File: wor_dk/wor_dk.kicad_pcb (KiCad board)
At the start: 4 copper layers, 108.7 x 57.5 mm, 140 parts, among them J101 Conn_01x02, J102 Conn_02x03_Odd_Even, J103 Conn_02x03_Odd_Even, J104 Conn_01x02, J201 SWD, J301 SMA, J302 Conn_02x04_Odd_Even, J303 Conn_02x06_Odd_Even, J401 USB_C_Receptacle_USB2.0_16P, J501 SWD, J502 USB_C_Receptacle_USB2.0_16P, J503 SWD, Q501 BSS84, SW201 SW_Push, SW501 SW_Push, U201 nRF52840, U202 TMUX1112PWR, U203 TMUX1112PWR, U301 Si4467, U401 FT232RL, U501 TLV1117-33, U502 LPC11U35FHI33_501, Y201 32.768kHz, Y202 32MHz, Y301 26MHz, Y501 12MHz

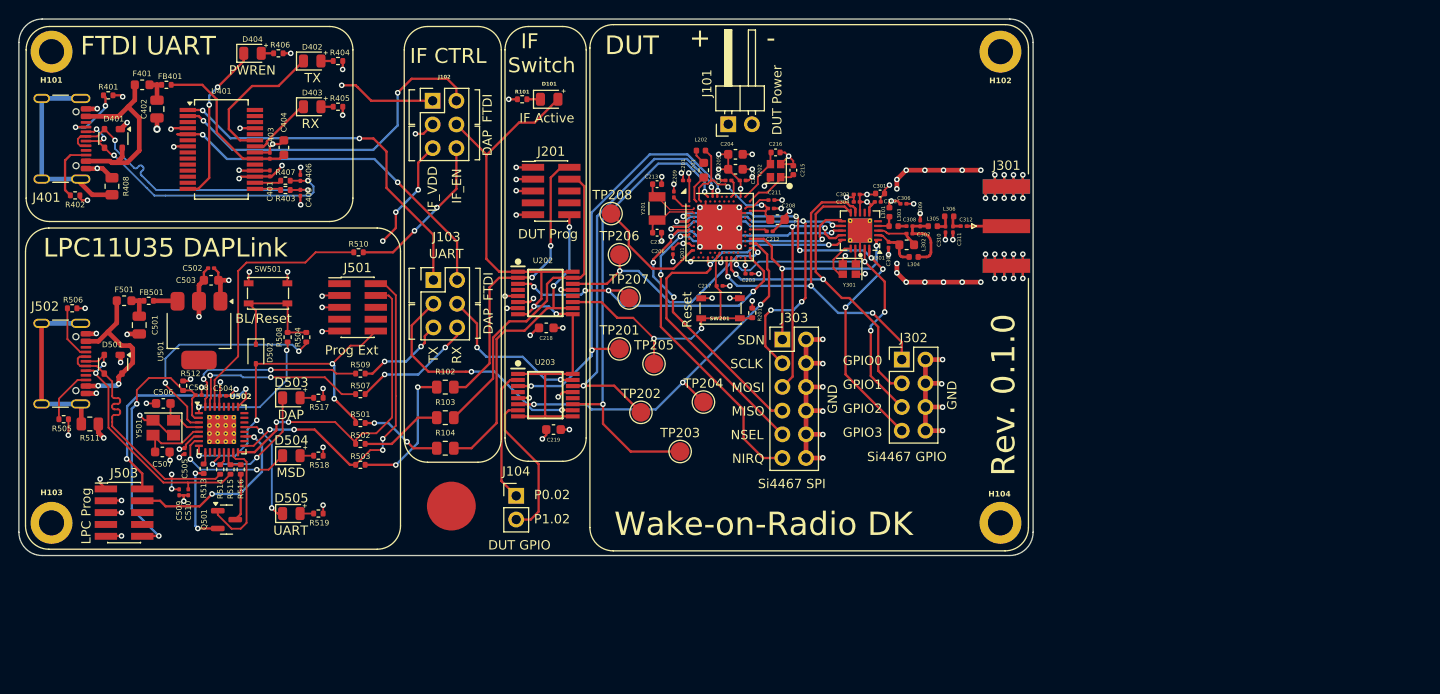
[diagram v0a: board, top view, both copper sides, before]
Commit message: wor_dk: PCB: adjust zone fills
- GND zone fill reduced to size of PCB
- VDD zone fills: chamfer corners
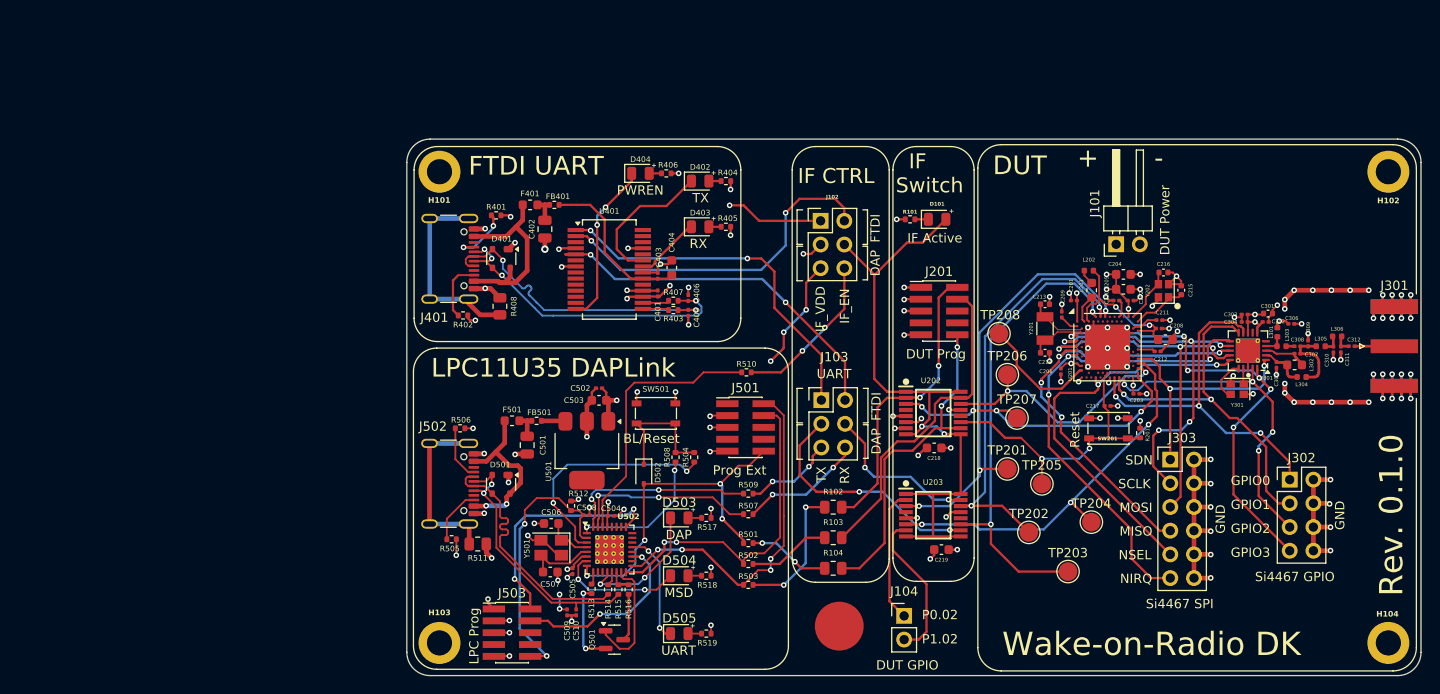
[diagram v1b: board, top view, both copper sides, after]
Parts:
- moved C213 43.5 mm to (165.4, 84.9)
- moved D504 43.5 mm to (126.2, 114.0)
- moved D505 43.5 mm to (126.2, 120.2)
- moved R510 43.5 mm to (133.4, 92.2)
- moved Y201 43.5 mm to (165.4, 87.5)
- moved H101 43.5 mm to (100.5, 70.7)
- moved H103 43.5 mm to (100.5, 121.2)
- moved C214 43.5 mm to (165.4, 90.1)
- moved C218 43.5 mm to (153.5, 100.3)
- moved D101 43.5 mm to (153.8, 75.8)
- moved D503 43.5 mm to (126.2, 107.8)
- moved FB401 43.5 mm to (112.8, 74.2)
- moved R401 43.5 mm to (106.6, 75.3)
- moved R406 43.5 mm to (124.8, 70.8)
- moved R514 43.5 mm to (118.6, 115.4)
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
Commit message: wor_dk: PCB: cleanup
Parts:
- moved TP203 5.01 mm to (163.1, 111.9)
- moved TP202 3.02 mm to (161.5, 107.2)
- moved R401 2.57 mm to (104.3, 74.1)
- moved TP205 1.00 mm to (166.0, 104.4)
- moved C404 0.84 mm to (125.3, 81.8)
- moved TP204 0.69 mm to (169.8, 107.8)
- moved L202 0.62 mm to (170.7, 81.3)
- moved J201 0.53 mm to (153.5, 85.6)
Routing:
- net /Main MCU/P0.31_: track 50.6 -> 43.6 mm
- net Net-(D402-K): track 15.6 -> 11.3 mm
- net /Main MCU/P0.29_: track 44.6 -> 40.6 mm
- net /LPC11U35 DAPLink Programmer/USB-SCON: track 13.1 -> 9.87 mm, vias 0 -> 2
- net /3V3_FTDI: track 20.1 -> 17.7 mm, vias 7 -> 6
- net /RXD_FTDI: track 39.9 -> 37.7 mm
- net /LPC11U35 DAPLink Programmer/IF_SWDIO: track 25.4 -> 23.7 mm
- net /Main MCU/SWCLK_: track 26.8 -> 25.6 mm
- net /Main MCU/SWDIO_: track 35.0 -> 33.8 mm
- net Net-(D404-K): track 17.7 -> 18.7 mm
- net Net-(J401-CC1): track 6.62 -> 7.64 mm, vias 2 -> 0
- net /Transceiver/MISO: track 47.2 -> 48.0 mm
- net /DTR_FTDI: track 37.3 -> 36.5 mm
- net /Main MCU/NRESET_: track 32.6 -> 33.3 mm
- net Net-(U401-VCC): track 17.6 -> 18.3 mm
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
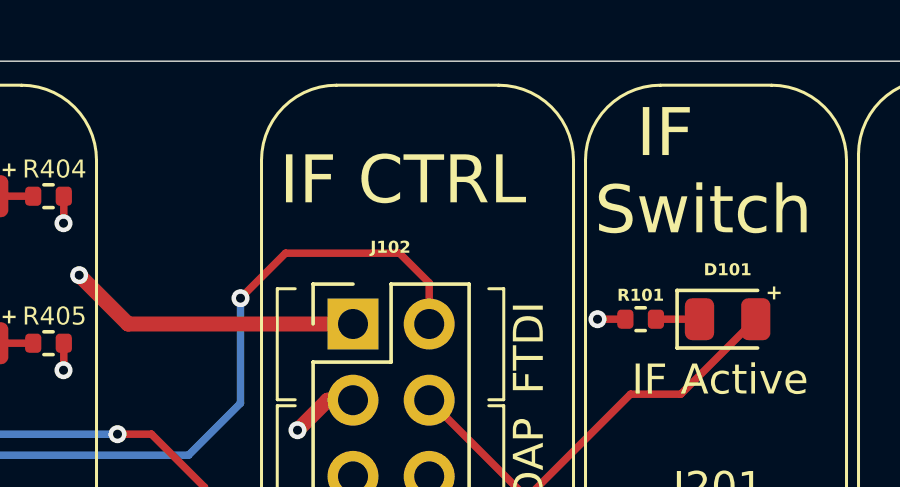
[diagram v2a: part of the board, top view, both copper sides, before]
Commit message: wor_dk: PCB: IF CTRL -> IF Control
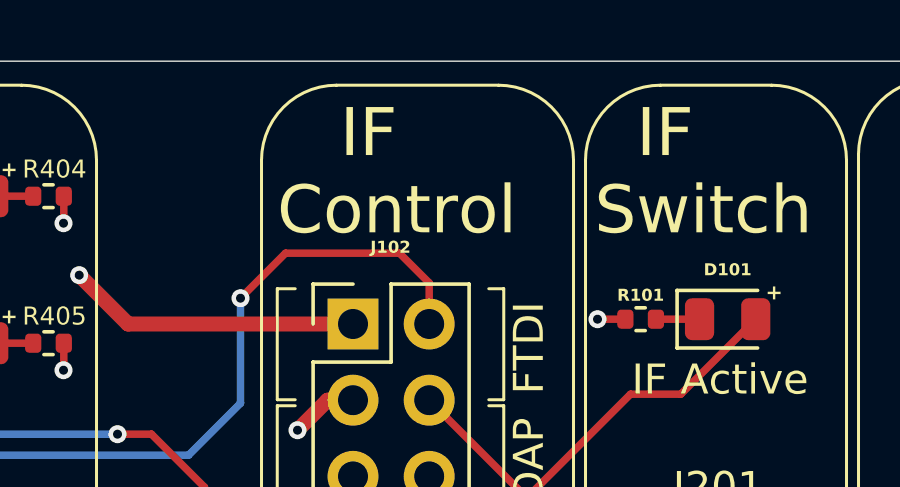
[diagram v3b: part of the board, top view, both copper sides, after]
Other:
- board text added: "IF Control"
- board text removed: "IF CTRL"
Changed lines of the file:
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@@
 		)
 	)
-	(gr_text "IF CTRL"
-		(at 138.877 72.0675 0)
+	(gr_text "   IF\nControl"
+		(at 138.8 73.0675 0)
 		(layer "F.SilkS")
 		(effects
